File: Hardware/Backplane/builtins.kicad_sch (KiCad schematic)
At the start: 39 parts, among them J1003 BM04B-SRSS-TB, J1004 BM04B-SRSS-TB, J1005 BM04B-SRSS-TB, J1006 BM04B-SRSS-TB, Q1004 S3134K, Q1005 S3134K, SW1001 Button 12mm, U1003 CD74HC221M96, U1004 PCF8523T/1,118, Y1001 32.768k

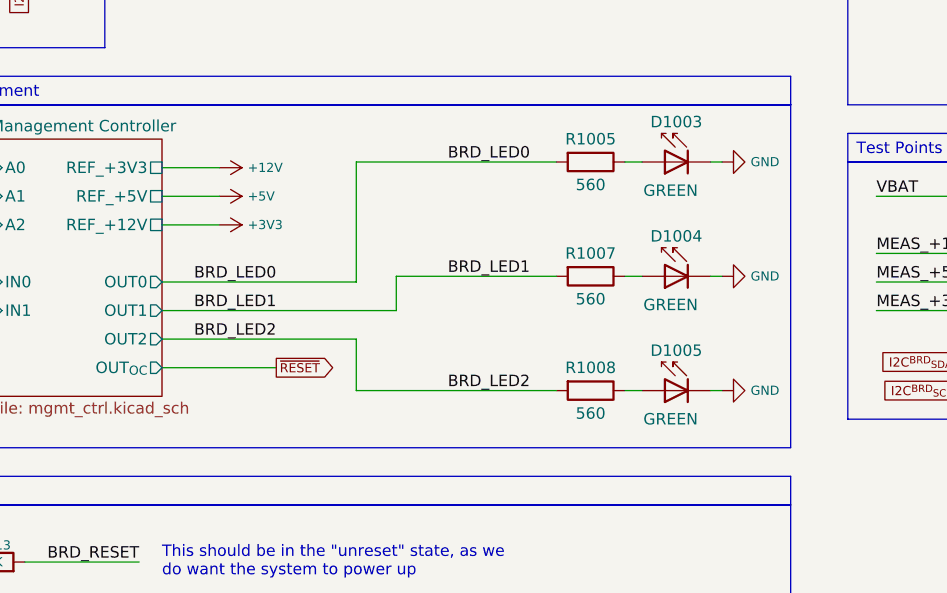
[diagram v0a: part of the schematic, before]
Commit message: Fixes two issues regarding the power supply of the TCA9548APWR, routes TCA9548APWR.RESET to the main board controller.
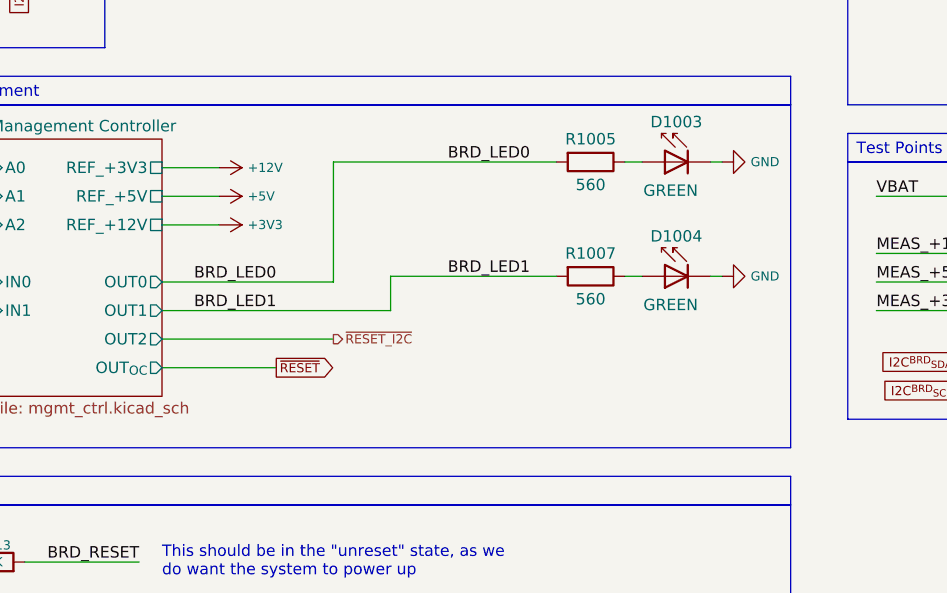
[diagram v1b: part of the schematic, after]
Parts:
- removed D1005: GREEN, LED_SMD:LED_0603_1608Metric, symbol LED:LD271
- removed R1008: 560, Resistor_SMD:R_0603_1608Metric, symbol Device:R
